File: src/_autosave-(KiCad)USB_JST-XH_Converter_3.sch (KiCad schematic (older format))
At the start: 15 parts

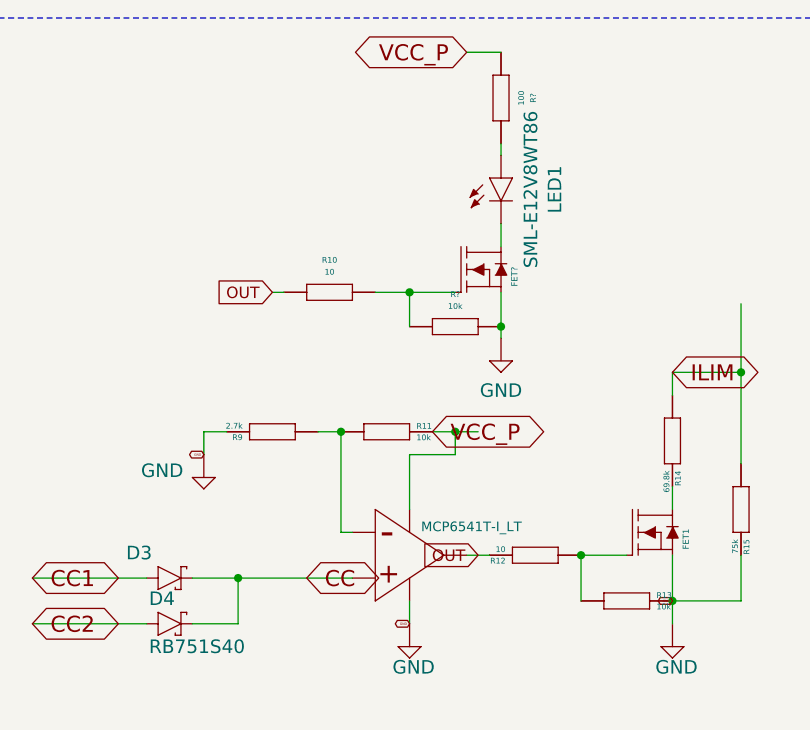
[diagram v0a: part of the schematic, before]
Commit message: 微修正、BJTのBS間抵抗の追加
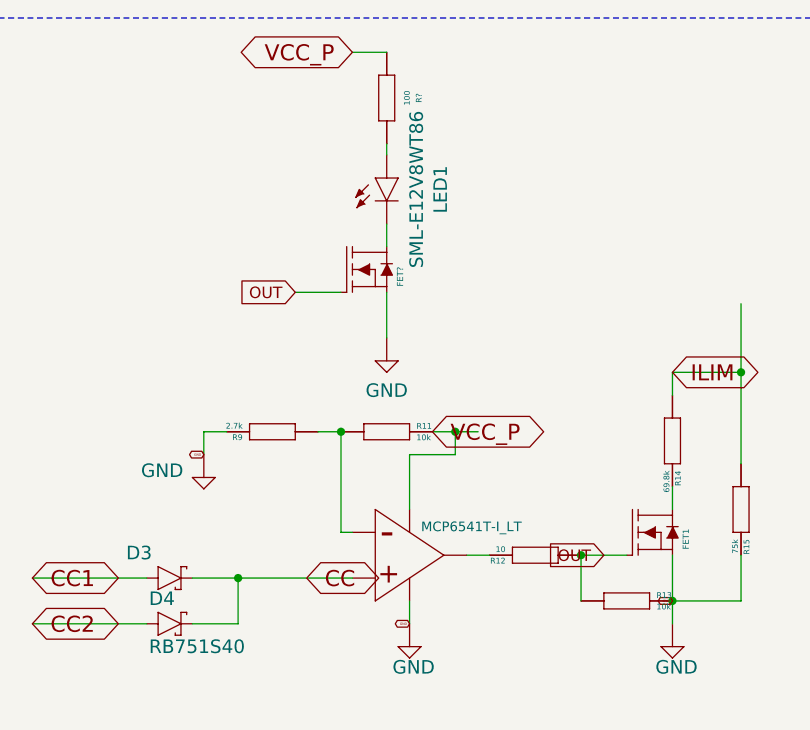
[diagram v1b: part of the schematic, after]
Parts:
- removed R10: 10, USB_JST-XH_Converter:RG2012, symbol USB_JST-XH_Converter-eagle-import:RG2012
- removed R?: 10k, USB_JST-XH_Converter:RG2012, symbol USB_JST-XH_Converter-eagle-import:RG2012
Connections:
- wire segments 38 -> 34
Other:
- moved on the sheet: FET?, LED1, R?
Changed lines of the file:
@@
 L USB_JST-XH_Converter-eagle-import:SML-E12V8WT86 LED1
 U 1 1 639EB85B
-P 6050 1850
-F 0 "LED1" V 6286 1800 59  0000 C CNN
-F 1 "SML-E12V8WT86" V 6181 1800 59  0000 C CNN
-F 2 "USB_JST-XH_Converter:SML-E12V8WT86" H 6050 1850 50  0001 C CNN
-F 3 "" H 6050 1850 50  0001 C CNN
-	1    6050 1850
+P 5550 1850
+F 0 "LED1" V 5786 1800 59  0000 C CNN
+F 1 "SML-E12V8WT86" V 5681 1800 59  0000 C CNN
+F 2 "USB_JST-XH_Converter:SML-E12V8WT86" H 5550 1850 50  0001 C CNN
+F 3 "" H 5550 1850 50  0001 C CNN
+	1    5550 1850
 	1    0    0    -1
 $EndComp
-Text GLabel 5950 3500 0    50   Input ~ 0
+Text GLabel 5150 2350 0    50   Input ~ 0
 OUT
-Text GLabel 5050 2350 0    50   Input ~ 0
-OUT
-$Comp
-L USB_JST-XH_Converter-eagle-import:RG2012 R10
-U 1 1 639F548F
-P 5300 2350
-F 0 "R10" H 5300 2491 25  0000 C CNN
-F 1 "10" H 5300 2439 25  0000 C CNN
-F 2 "USB_JST-XH_Converter:RG2012" H 5300 2350 50  0001 C CNN
-F 3 "" H 5300 2350 50  0001 C CNN
-	1    5300 2350
-	1    0    0    -1
-$EndComp
 $Comp
 L USB_JST-XH_Converter-eagle-import:GND #SUPPLY0114
 U 1 1 639F6F3D
-P 6050 2650
-F 0 "#SUPPLY0114" H 6050 2650 50  0001 C CNN
-F 1 "GND" H 6050 2520 59  0000 C CNN
-F 2 "" H 6050 2650 50  0001 C CNN
-F 3 "" H 6050 2650 50  0001 C CNN
-	1    6050 2650
+P 5550 2650
+F 0 "#SUPPLY0114" H 5550 2650 50  0001 C CNN
+F 1 "GND" H 5550 2520 59  0000 C CNN
+F 2 "" H 5550 2650 50  0001 C CNN
+F 3 "" H 5550 2650 50  0001 C CNN
+	1    5550 2650
 	1    0    0    -1
 $EndComp
@@
 L USB_JST-XH_Converter-eagle-import:BSS138 FET?
 U 1 1 63A1C7C7
-P 6050 2250
+P 5550 2250
 AR Path="/63A1C7C7" Ref="FET?"  Part="1"
 AR Path="/639B4E7B/63A1C7C7" Ref="FET?"  Part="1"
 AR Path="/639ECBA2/63A1C7C7" Ref="FET?"  Part="1"
-F 0 "FET?" V 6125 2175 27  0000 L BNN
-F 1 "BSS138" H 6050 2250 50  0001 C CNN
-F 2 "USB_JST-XH_Converter:SOT-23" H 6050 2250 50  0001 C CNN
-F 3 "" H 6050 2250 50  0001 C CNN
-	1    6050 2250
+F 0 "FET?" V 5625 2175 27  0000 L BNN
+F 1 "BSS138" H 5550 2250 50  0001 C CNN
+F 2 "USB_JST-XH_Converter:SOT-23" H 5550 2250 50  0001 C CNN
+F 3 "" H 5550 2250 50  0001 C CNN
+	1    5550 2250
 	1    0    0    -1
 $EndComp
-Wire Wire Line
-	5100 2350 5050 2350
-Wire Wire Line
-	5500 2350 5650 2350
-$Comp
-L USB_JST-XH_Converter-eagle-import:RG2012 R?
-U 1 1 63A2188D
-P 5850 2500
-F 0 "R?" H 5850 2641 25  0000 C CNN
-F 1 "10k" H 5850 2589 25  0000 C CNN
-F 2 "USB_JST-XH_Converter:RG2012" H 5850 2500 50  0001 C CNN
-F 3 "" H 5850 2500 50  0001 C CNN
-	1    5850 2500
-	1    0    0    -1
-$EndComp
-Wire Wire Line
-	5650 2500 5650 2350
-Connection ~ 5650 2350
-Wire Wire Line
-	5650 2350 5850 2350
-Wire Wire Line
-	6050 2500 6050 2550
-Wire Wire Line
-	6050 2500 6050 2350
-Connection ~ 6050 2500
 $Comp
 L USB_JST-XH_Converter-eagle-import:RG2012 R?
 U 1 1 63A28D93
-P 6050 1500
-F 0 "R?" H 6050 1641 25  0000 C CNN
-F 1 "100" H 6050 1589 25  0000 C CNN
-F 2 "USB_JST-XH_Converter:RG2012" H 6050 1500 50  0001 C CNN
-F 3 "" H 6050 1500 50  0001 C CNN
-	1    6050 1500
+P 5550 1500
+F 0 "R?" H 5550 1641 25  0000 C CNN
+F 1 "100" H 5550 1589 25  0000 C CNN
+F 2 "USB_JST-XH_Converter:RG2012" H 5550 1500 50  0001 C CNN
+F 3 "" H 5550 1500 50  0001 C CNN
+	1    5550 1500
 	0    1    1    0
 $EndComp
 Wire Wire Line
-	6050 1700 6050 1750
+	5550 1700 5550 1750
 Wire Wire Line
-	6050 2050 6050 2150
-Text GLabel 5900 1300 0    70   BiDi ~ 0
+	5550 2050 5550 2150
+Text GLabel 5400 1300 0    70   BiDi ~ 0
 VCC_P
 Wire Wire Line
-	6050 1300 5900 1300
+	5550 1300 5400 1300
+Wire Wire Line
+	5550 2350 5550 2550
+Wire Wire Line
+	5150 2350 5350 2350
+Text GLabel 6500 3500 0    50   Input ~ 0
+OUT
 $EndSCHEMATC
